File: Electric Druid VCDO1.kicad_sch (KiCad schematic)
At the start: 2 parts, among them J12 Control_board, J13 Main_board

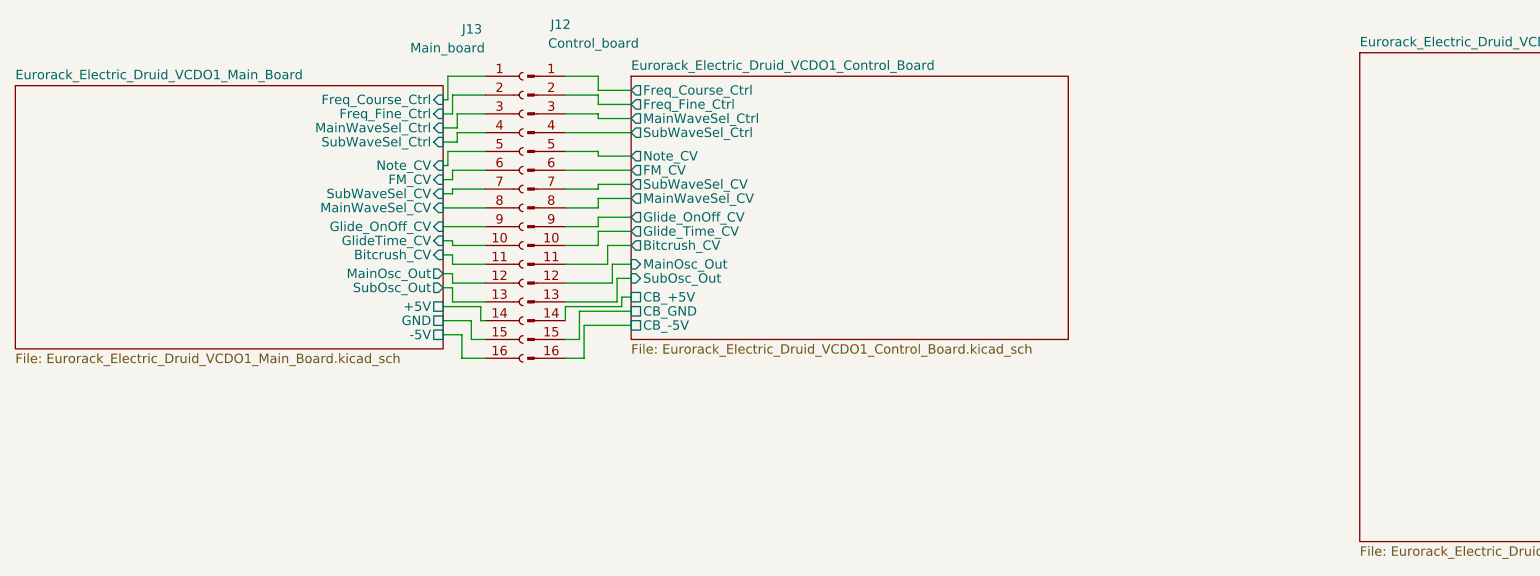
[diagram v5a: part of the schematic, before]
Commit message: updated schematic to rev 0.1.1
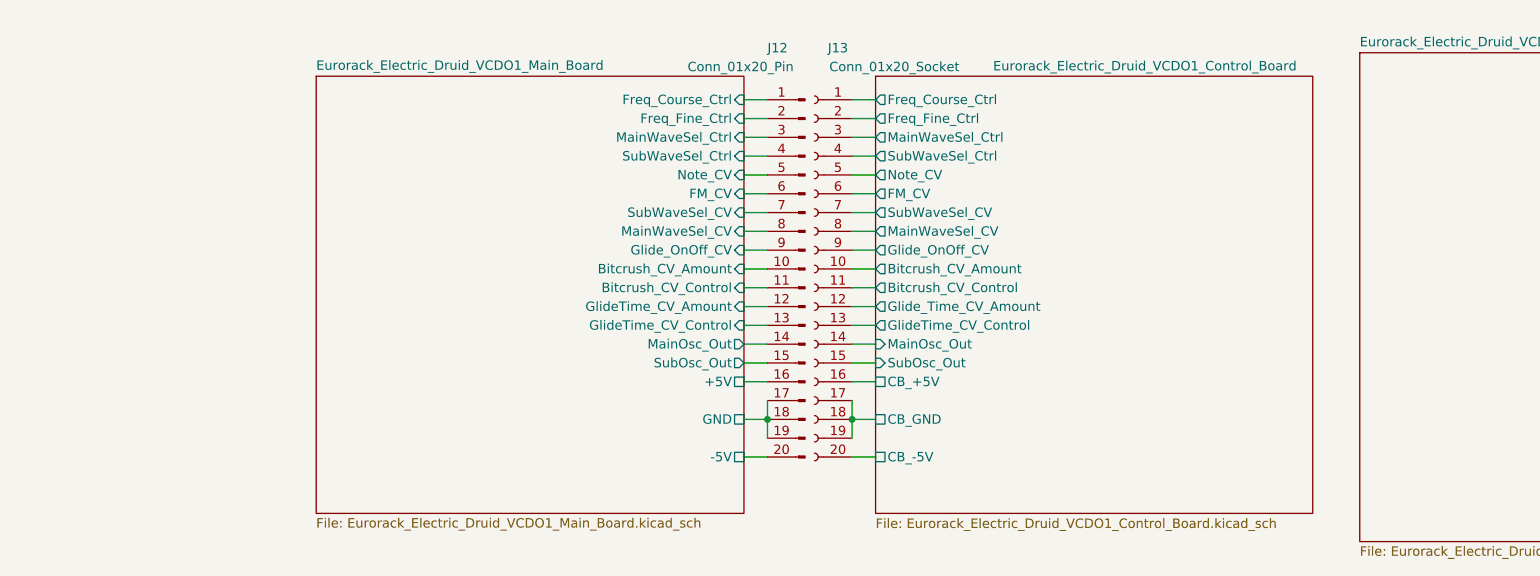
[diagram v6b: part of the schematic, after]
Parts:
- removed J12: Control_board, Connector_PinHeader_2.54mm:PinHeader_1x16_P2.54mm_Vertical, symbol Connector:Conn_01x16_Pin
- removed J13: Main_board, Connector_PinSocket_2.54mm:PinSocket_1x16_P2.54mm_Vertical, symbol Connector:Conn_01x16_Socket
- added J12: Conn_01x20_Pin, symbol Connector:Conn_01x20_Pin
- added J13: Conn_01x20_Socket, symbol Connector:Conn_01x20_Socket
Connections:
- net Eurorack_Electric_Druid_VCDO1_Control_Board/CB_+5V: now also J13.16 (Pin_16)
- net Eurorack_Electric_Druid_VCDO1_Control_Board/CB_-5V: now also J13.20 (Pin_20)
- net Eurorack_Electric_Druid_VCDO1_Control_Board/CB_GND: now also J13.17 (Pin_17), J13.18 (Pin_18), J13.19 (Pin_19)
- net Eurorack_Electric_Druid_VCDO1_Control_Board/FM_CV: now also J13.6 (Pin_6)
- net Eurorack_Electric_Druid_VCDO1_Control_Board/Freq_Course_Ctrl: now also J13.1 (Pin_1)
- net Eurorack_Electric_Druid_VCDO1_Control_Board/Freq_Fine_Ctrl: now also J13.2 (Pin_2)
- net Eurorack_Electric_Druid_VCDO1_Control_Board/Glide_OnOff_CV: now also J13.9 (Pin_9)
- net Eurorack_Electric_Druid_VCDO1_Control_Board/MainOsc_Out: now also J13.14 (Pin_14)
- net Eurorack_Electric_Druid_VCDO1_Control_Board/MainWaveSel_CV: now also J13.8 (Pin_8)
- net Eurorack_Electric_Druid_VCDO1_Control_Board/MainWaveSel_Ctrl: now also J13.3 (Pin_3)
- net Eurorack_Electric_Druid_VCDO1_Control_Board/Note_CV: now also J13.5 (Pin_5)
- net Eurorack_Electric_Druid_VCDO1_Control_Board/SubOsc_Out: now also J13.15 (Pin_15)
- net Eurorack_Electric_Druid_VCDO1_Control_Board/SubWaveSel_CV: now also J13.7 (Pin_7)
- net Eurorack_Electric_Druid_VCDO1_Control_Board/SubWaveSel_Ctrl: now also J13.4 (Pin_4)
- net Eurorack_Electric_Druid_VCDO1_Main_Board/+5V: now also J12.16 (Pin_16)
- net Eurorack_Electric_Druid_VCDO1_Main_Board/-5V: now also J12.20 (Pin_20)
- net Eurorack_Electric_Druid_VCDO1_Main_Board/FM_CV: now also J12.6 (Pin_6)
- net Eurorack_Electric_Druid_VCDO1_Main_Board/Freq_Course_Ctrl: now also J12.1 (Pin_1)
- net Eurorack_Electric_Druid_VCDO1_Main_Board/Freq_Fine_Ctrl: now also J12.2 (Pin_2)
- net Eurorack_Electric_Druid_VCDO1_Main_Board/GND: now also J12.17 (Pin_17), J12.18 (Pin_18), J12.19 (Pin_19)
- net Eurorack_Electric_Druid_VCDO1_Main_Board/Glide_OnOff_CV: now also J12.9 (Pin_9)
- net Eurorack_Electric_Druid_VCDO1_Main_Board/MainOsc_Out: now also J12.14 (Pin_14)
- net Eurorack_Electric_Druid_VCDO1_Main_Board/MainWaveSel_CV: now also J12.8 (Pin_8)
- net Eurorack_Electric_Druid_VCDO1_Main_Board/MainWaveSel_Ctrl: now also J12.3 (Pin_3)
- net Eurorack_Electric_Druid_VCDO1_Main_Board/Note_CV: now also J12.5 (Pin_5)
- net Eurorack_Electric_Druid_VCDO1_Main_Board/SubOsc_Out: now also J12.15 (Pin_15)
- net Eurorack_Electric_Druid_VCDO1_Main_Board/SubWaveSel_CV: now also J12.7 (Pin_7)
- net Eurorack_Electric_Druid_VCDO1_Main_Board/SubWaveSel_Ctrl: now also J12.4 (Pin_4)
- new net Eurorack_Electric_Druid_VCDO1_Control_Board/Bitcrush_CV_Amount: J13.10 (Pin_10)
- new net Eurorack_Electric_Druid_VCDO1_Control_Board/Bitcrush_CV_Control: J13.11 (Pin_11)
- new net Eurorack_Electric_Druid_VCDO1_Control_Board/GlideTime_CV_Control: J13.13 (Pin_13)
- new net Eurorack_Electric_Druid_VCDO1_Control_Board/Glide_Time_CV_Amount: J13.12 (Pin_12)
- new net Eurorack_Electric_Druid_VCDO1_Main_Board/Bitcrush_CV_Amount: J12.10 (Pin_10)
- new net Eurorack_Electric_Druid_VCDO1_Main_Board/Bitcrush_CV_Control: J12.11 (Pin_11)
- new net Eurorack_Electric_Druid_VCDO1_Main_Board/GlideTime_CV_Amount: J12.12 (Pin_12)
- new net Eurorack_Electric_Druid_VCDO1_Main_Board/GlideTime_CV_Control: J12.13 (Pin_13)
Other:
- sheet Eurorack_Electric_Druid_VCDO1_Control_Board ports: added Bitcrush_CV_Amount, Bitcrush_CV_Control, GlideTime_CV_Control, Glide_Time_CV_Amount; removed Bitcrush_CV, Glide_Time_CV
- sheet Eurorack_Electric_Druid_VCDO1_Main_Board ports: added Bitcrush_CV_Amount, Bitcrush_CV_Control, GlideTime_CV_Amount, GlideTime_CV_Control; removed Bitcrush_CV, GlideTime_CV

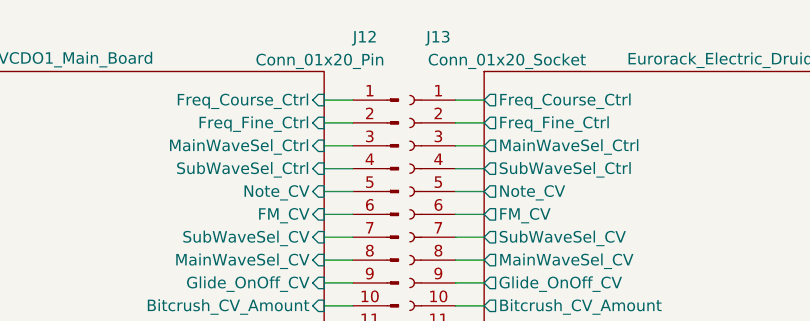
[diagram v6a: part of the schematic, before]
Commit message: updated to schematic revision 1.2
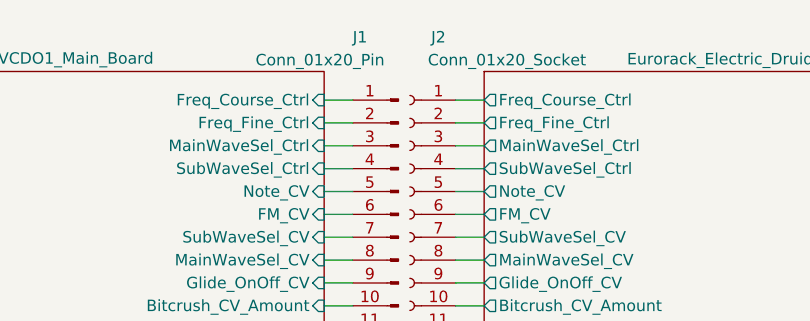
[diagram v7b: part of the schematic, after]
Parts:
- renumbered J12 to J1, J13 to J2
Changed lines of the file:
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@@
     (title "Eurorack Electric Druid VCDO1 - Root Sheet")
     (date "2023-12-30")
-    (rev "0.1.1")
+    (rev "0.1.2")
     (company "DIYSynthMNL")
     (comment 1 "Shared under a CC BY-NC-SA 4.0 license. Some rights reserved.")
@@
   (symbol (lib_id "Connector:Conn_01x20_Pin") (at 140.335 88.9 0) (mirror y) (unit 1)
     (in_bom yes) (on_board yes) (dnp no)
-    (property "Reference" "J12" (at 135.255 59.055 0)
+    (property "Reference" "J1" (at 135.255 59.055 0)
       (effects (font (size 1.27 1.27)) (justify right))
     )
@@
       (project "Electric Druid VCDO1"
         (path "/1a79e409-2950-446e-9b6e-16f6bf0a888d"
-          (reference "J12") (unit 1)
+          (reference "J1") (unit 1)
         )
       )
@@
   (symbol (lib_id "Connector:Conn_01x20_Socket") (at 141.605 88.9 0) (mirror y) (unit 1)
     (in_bom yes) (on_board yes) (dnp no)
-    (property "Reference" "J13" (at 144.78 59.055 0)
+    (property "Reference" "J2" (at 144.78 59.055 0)
       (effects (font (size 1.27 1.27)))
     )
@@
       (project "Electric Druid VCDO1"
         (path "/1a79e409-2950-446e-9b6e-16f6bf0a888d"
-          (reference "J13") (unit 1)
+          (reference "J2") (unit 1)
         )
       )
